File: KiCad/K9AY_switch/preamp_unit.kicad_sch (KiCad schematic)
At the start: 24 parts, among them J6 RF_OUT, K11 TIANBO-HJR-4102-L, K12 TIANBO-HJR-4102-L, Q1 MMBFJ310, Q4 MMBFJ310, Q5 IRLML5203

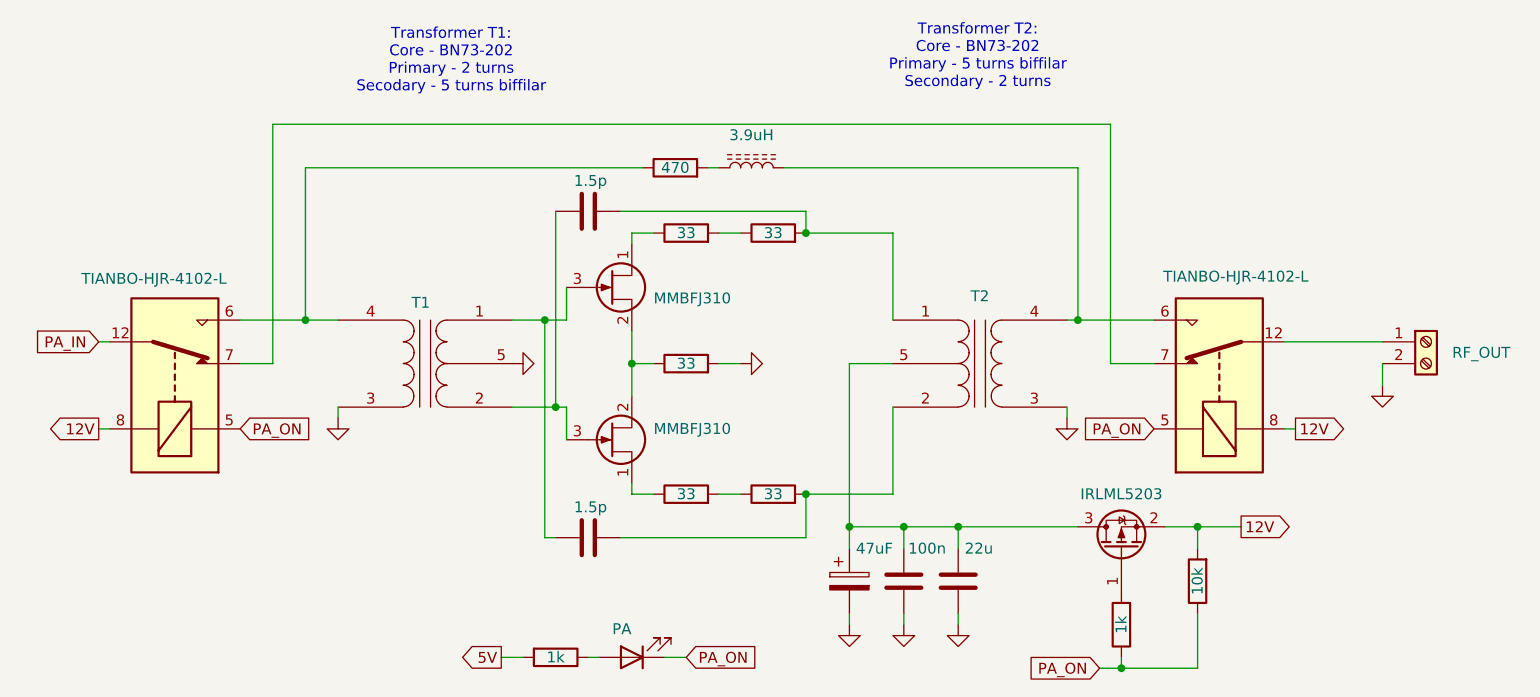
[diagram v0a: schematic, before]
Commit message: Update KiCad project, gerbers and pictures
- updated schematic, PCB, BOM, gerbers and plots
- new photos: k1, mosfet, pwr; updated direction diagram
- ignore KiCad backups, *.tar.gz and k9ay_v5.zip

Co-Authored-By: Claude Opus 5.5 <noreply@anthropic.com>
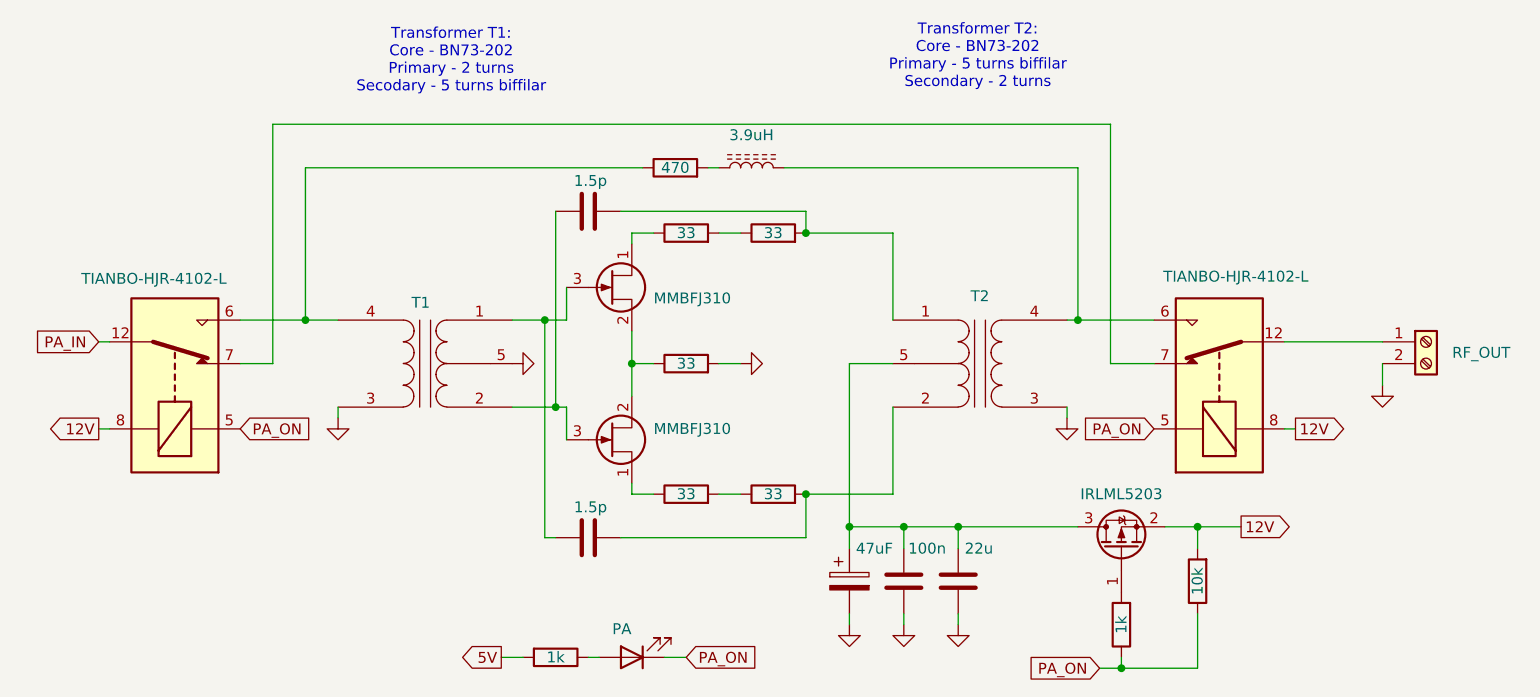
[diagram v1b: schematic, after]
